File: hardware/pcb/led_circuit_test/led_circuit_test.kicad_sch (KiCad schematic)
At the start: 23 parts, among them J1 Conn_01x01_Male, J2 Conn_01x01_Male, J3 Conn_01x01_Male, J4 Conn_01x01_Male, J5 Conn_01x01_Male, J6 Conn_01x01_Male

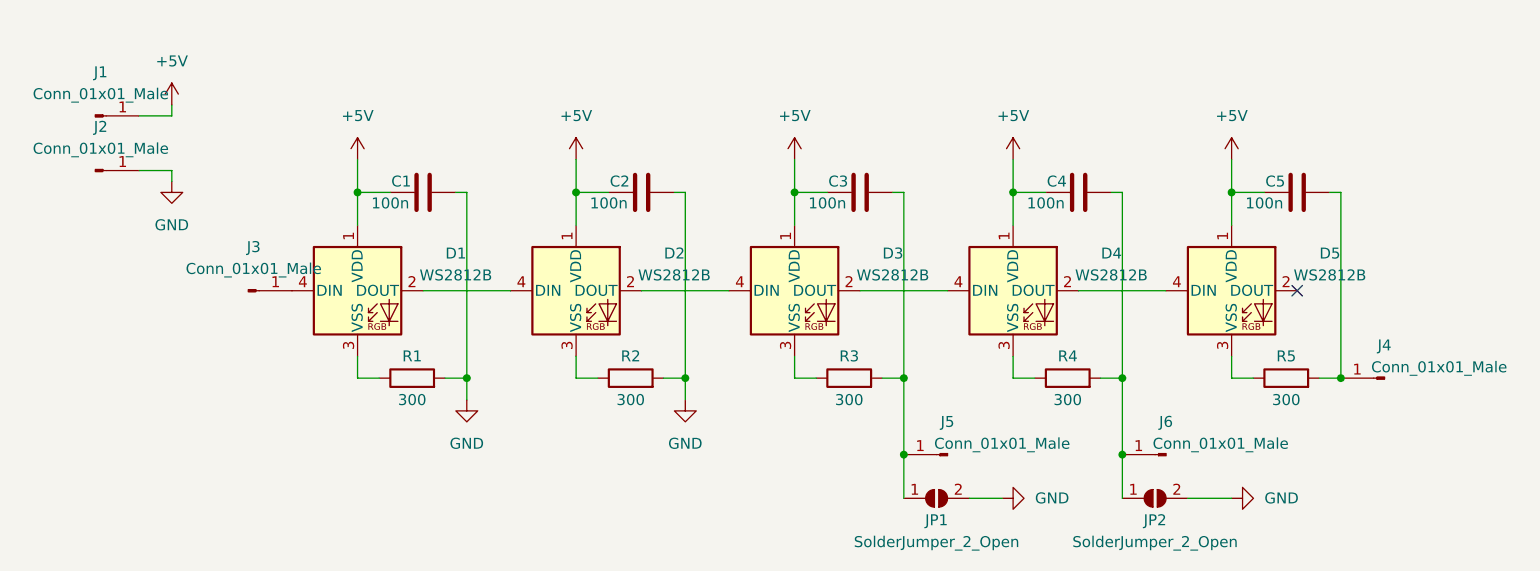
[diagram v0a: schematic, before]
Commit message: Updated and enhanced test PCB after testing
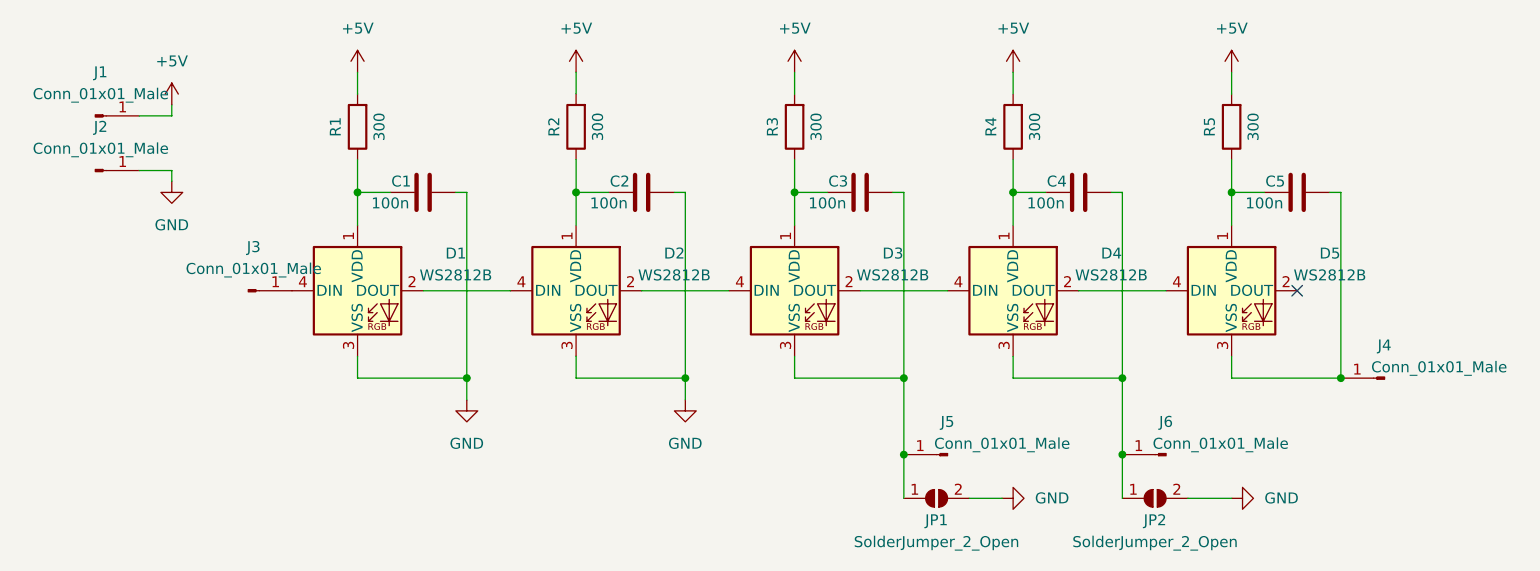
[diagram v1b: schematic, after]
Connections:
- net +5V: now also R1.2, R2.2, R3.2, R4.2, R5.2; no longer C1.1, C2.1, C3.1, C4.1, C5.1, D1.1 (VDD), D2.1 (VDD), D3.1 (VDD), D4.1 (VDD), D5.1 (VDD)
- net GND: now also D1.3 (VSS), D2.3 (VSS); no longer R1.2, R2.2
- net at R2.1: now also C2.1, D2.1 (VDD); no longer D2.3 (VSS)
- net at R1.1: now also C1.1, D1.1 (VDD); no longer D1.3 (VSS)
- net at C3.2, J5.1 (Pin_1), JP1.1 (A): now also D3.3 (VSS); no longer R3.2
- net at C5.2, J4.1 (Pin_1): now also D5.3 (VSS); no longer R5.2
- net at R4.1: now also C4.1, D4.1 (VDD); no longer D4.3 (VSS)
- net at C4.2, J6.1 (Pin_1), JP2.1 (A): now also D4.3 (VSS); no longer R4.2
- net at R3.1: now also C3.1, D3.1 (VDD); no longer D3.3 (VSS)
- net at R5.1: now also C5.1, D5.1 (VDD); no longer D5.3 (VSS)
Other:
- moved on the sheet: R1, R2, R3, R4, R5
